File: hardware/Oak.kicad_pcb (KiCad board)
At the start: 2 copper layers, 100 x 40 mm, 69 parts, among them J1 18650 Battery holder, J2 USB_B_Micro, J4 Conn_ARM_JTAG_SWD_10, SW1 SW_SPDT, SW2 SW_Push, U1 AP2112, U2 ATSAMD21, U3 MCP7383, U4 PA1010D, U5 RFM95, U6 Waveshare_1in54_epaper

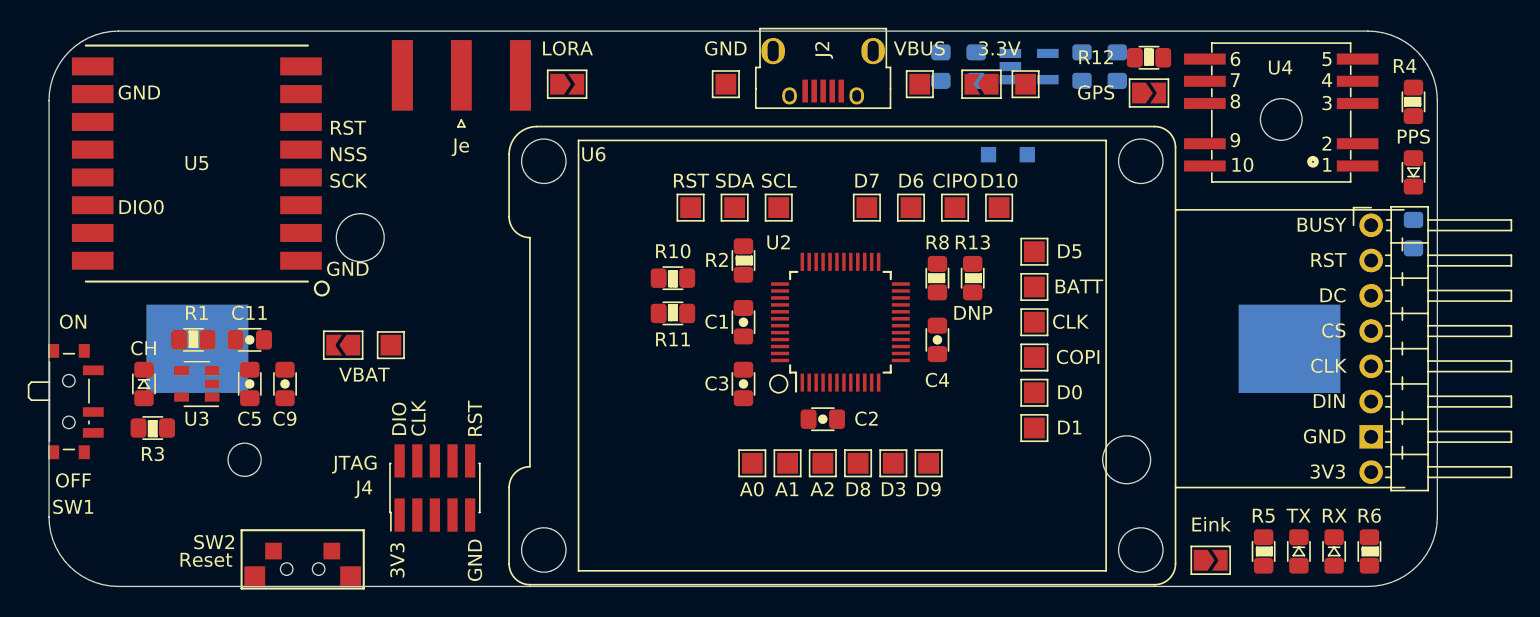
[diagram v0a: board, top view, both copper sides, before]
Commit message: feat: fix all clearance issues with local clearance settings
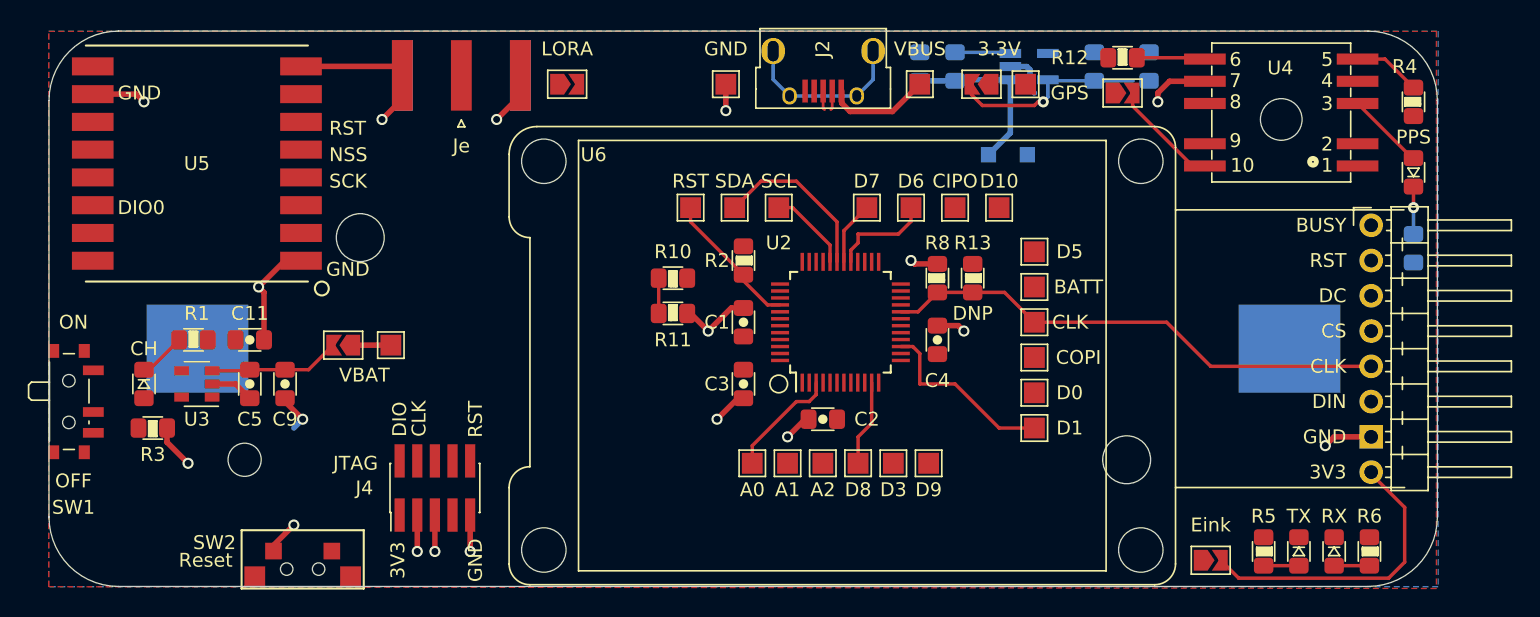
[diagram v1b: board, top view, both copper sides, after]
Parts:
- moved C7 2.29 mm to (172.7, 72.4)
- moved JP3 1.91 mm to (170.8, 74.3)
- moved R12 1.91 mm to (170.8, 71.8)
- moved C10 1.52 mm to (156.2, 72.4)
- moved R9 1.52 mm to (158.8, 72.4)
- moved R7 1.03 mm to (191.8, 85.5)
- moved C6 0.89 mm to (168.8, 72.4)
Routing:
- net GND: track 0.00 -> 73.1 mm, vias 0 -> 18
- net /CLK: track 0.00 -> 36.7 mm
- net Net-(JP5-Pad2): track 0.00 -> 21.7 mm
- net /VBUS: track 0.00 -> 20.2 mm
- net Net-(C6-Pad1): track 0.00 -> 14.3 mm, vias 0 -> 1
- net /D1: track 0.00 -> 13.3 mm
- net Net-(J2-Pad6): track 0.00 -> 12.3 mm
- net /SDA: track 0.00 -> 12.3 mm
- net /RST: track 0.00 -> 10.2 mm
- net Net-(C5-Pad2): track 0.00 -> 9.48 mm
- net /A0: track 0.00 -> 8.25 mm
- net Net-(JP3-Pad2): track 0.00 -> 7.93 mm
- net /D6: track 0.00 -> 7.40 mm
- net /D8: track 0.00 -> 6.22 mm
- net /SCL: track 0.00 -> 6.02 mm
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- added copper zone on F.Cu, net +3V3
- added copper zone on B.Cu, net GND

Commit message: feat: add inverted labels with more routes (33 unconnected). close #18
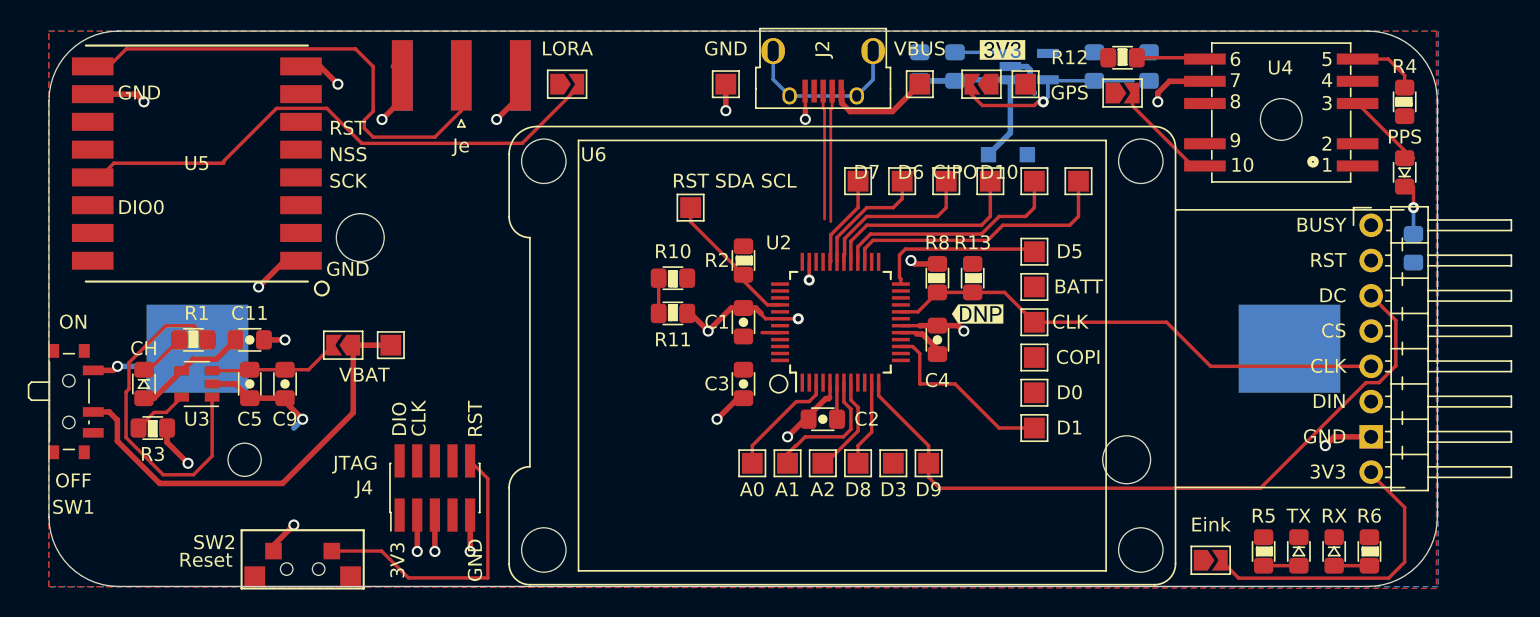
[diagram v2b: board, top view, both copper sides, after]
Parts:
- added svg2mod: G***, label, F.Cu at (160.4, 90.2)
- added svg2mod: G***, label, F.Cu at (162.2, 71.2)
- moved TP17 12.2 mm to (154.9, 80.6)
- moved TP19 6.02 mm to (158.1, 80.6)
- moved TP20 6.02 mm to (161.3, 80.6)
- moved TP21 6.02 mm to (164.5, 80.6)
- moved TP18 6.02 mm to (151.8, 80.6)
- moved TP22 6.02 mm to (167.6, 80.6)
- moved D3 0.64 mm to (191.1, 80.0)
- moved R4 0.64 mm to (191.1, 74.9)
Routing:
- net /D9: track 0.00 -> 51.7 mm
- net Net-(JP4-Pad2): track 0.00 -> 39.5 mm
- net Net-(J3-Pad1): track 0.00 -> 36.0 mm
- net /VBAT: track 2.70 -> 31.4 mm
- net Net-(R1-Pad2): track 0.00 -> 24.8 mm
- net /RST: track 10.2 -> 31.2 mm
- net /D10: track 0.00 -> 19.8 mm
- net /CIPO: track 0.00 -> 16.9 mm
- net /D5: track 0.00 -> 12.1 mm
- net /A1: track 0.00 -> 9.55 mm
- net GND: track 73.1 -> 82.4 mm, vias 18 -> 23
- net /VBUS: track 20.2 -> 28.5 mm
- net Net-(J1-Pad1): track 0.00 -> 8.15 mm, vias 0 -> 1
- net /USB_D-: track 1.38 -> 9.45 mm
- net /USB_D+: track 1.38 -> 9.26 mm
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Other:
- net class Power: clearance 0.3 -> 0.2
- board text removed: "3.3V"
- board text removed: "DNP"

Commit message: feat: add more routes (22 remaining unconnected)
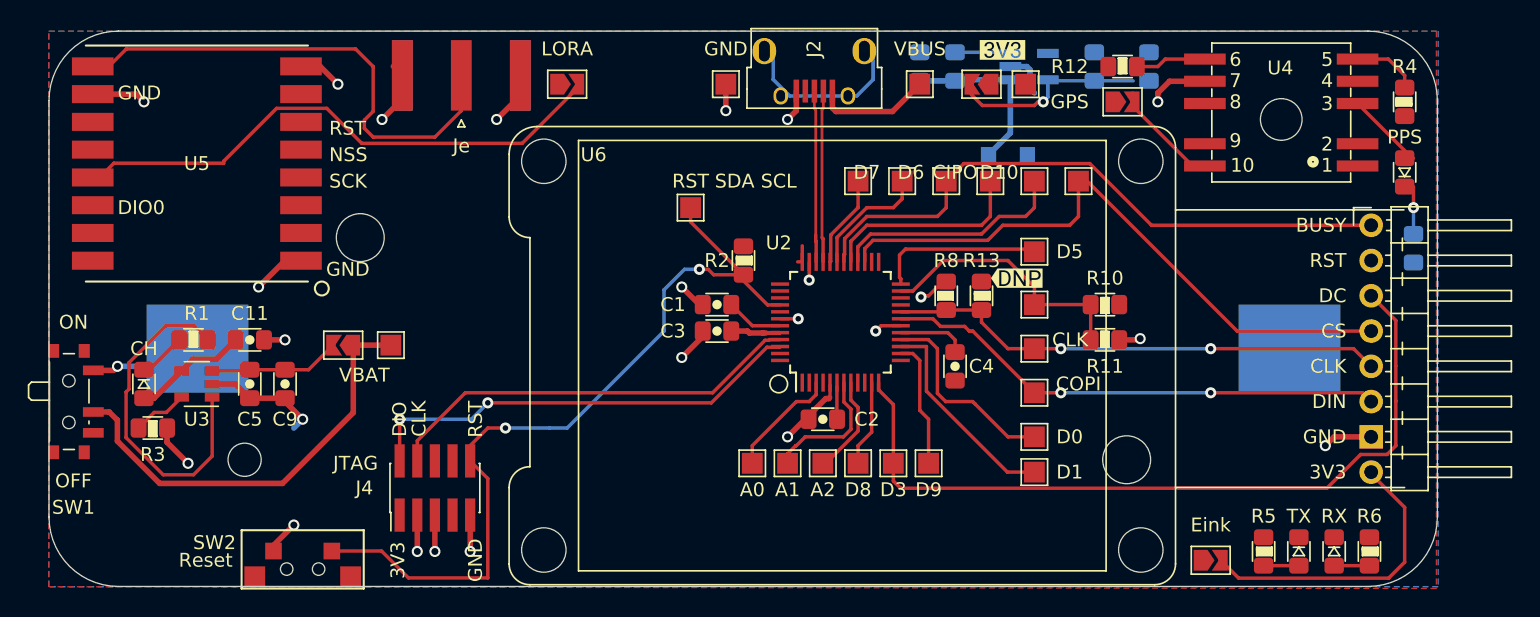
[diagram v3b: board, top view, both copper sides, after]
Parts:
- moved R10 31.2 mm to (169.5, 89.5)
- moved R11 31.2 mm to (169.5, 92.1)
- moved C3 4.26 mm to (141.6, 91.4), turned to 180 degrees
- moved svg2mod 3.82 mm to (163.2, 87.6)
- moved TP12 3.17 mm to (164.5, 101.6)
- moved TP13 3.17 mm to (164.5, 99.1)
- moved TP5 2.54 mm to (164.5, 95.9)
- moved TP10 2.54 mm to (154.3, 101.0)
- moved TP11 2.54 mm to (156.8, 101.0)
- moved C1 2.29 mm to (141.6, 89.5), turned to 0 degrees
- moved C4 2.29 mm to (158.8, 94.0), turned to 270 degrees
- moved TP16 1.90 mm to (164.5, 92.7)
- moved R8 1.42 mm to (158.1, 88.9)
- moved R13 1.42 mm to (160.7, 88.9)
- moved TP14 1.27 mm to (164.5, 89.5)
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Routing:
- net /COPI: track 0.00 -> 36.3 mm, vias 0 -> 2
- net /D7: track 11.8 -> 44.8 mm
- net /SWDIO: track 0.00 -> 32.6 mm, vias 0 -> 2
- net /SWCLK: track 0.00 -> 30.6 mm
- net /RST: track 31.2 -> 59.1 mm, vias 0 -> 2
- net /D10: track 19.8 -> 45.4 mm
- net /BATT: track 2.54 -> 19.2 mm
- net /D0: track 0.00 -> 14.4 mm
- net /D3: track 4.94 -> 14.5 mm
- net +3V3: track 6.76 -> 13.6 mm
- net GND: track 82.4 -> 76.7 mm, vias 23 -> 24
- net /D9: track 51.7 -> 56.7 mm
- net Net-(C1-Pad2): track 0.00 -> 4.14 mm
- net /USB_D+: track 9.26 -> 12.4 mm
- net /USB_D-: track 9.45 -> 12.4 mm
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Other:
- board text removed: "BATT"

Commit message: feat: add more routes (14 remaining unconnected)
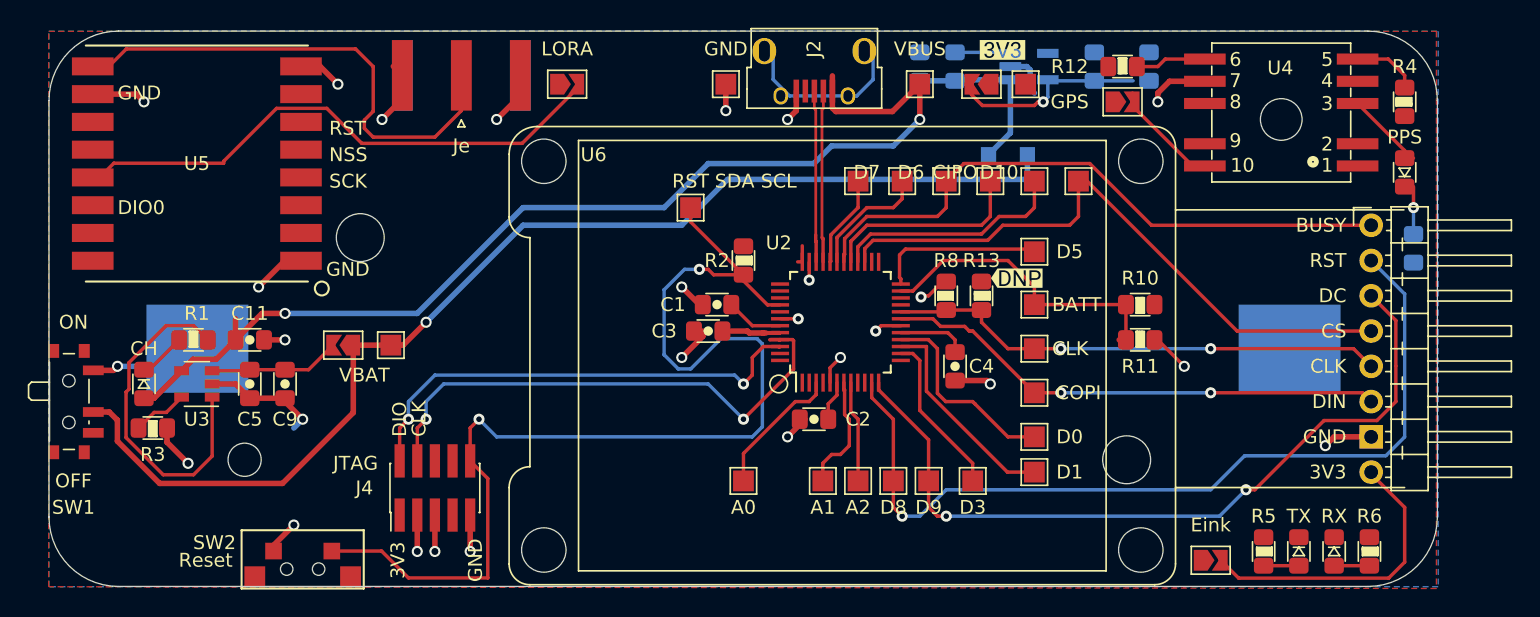
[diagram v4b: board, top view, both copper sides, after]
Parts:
- moved TP11 3.42 mm to (160.0, 102.2)
- moved TP9 2.84 mm to (154.3, 102.2)
- moved TP10 2.84 mm to (156.8, 102.2)
- moved TP6 2.84 mm to (151.8, 102.2)
- moved TP7 2.84 mm to (149.2, 102.2)
- moved R10 2.54 mm to (172.1, 89.5)
- moved R11 2.54 mm to (172.1, 92.1)
- moved TP8 1.42 mm to (143.5, 102.2)
- moved C2 0.63 mm to (148.6, 97.8)
- moved C3 0.63 mm to (141.0, 91.4)
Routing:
- net /VBUS: track 29.4 -> 90.4 mm, vias 0 -> 2
- net /D8: track 6.22 -> 62.8 mm, vias 0 -> 1
- net /VBAT: track 31.4 -> 84.0 mm, vias 0 -> 1
- net /RST: track 59.1 -> 82.5 mm
- net /SWCLK: track 30.6 -> 37.9 mm, vias 0 -> 2
- net /BATT: track 19.2 -> 22.0 mm
- net /D3: track 14.5 -> 17.1 mm
- net GND: track 76.7 -> 79.2 mm, vias 24 -> 26
- net /SWDIO: track 32.6 -> 34.3 mm
- net /A0: track 8.25 -> 9.83 mm
- net /A1: track 9.55 -> 8.40 mm
- net +3V3: track 13.6 -> 14.6 mm
- net /D9: track 56.7 -> 56.1 mm, vias 0 -> 2
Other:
- board text added: "BATT"

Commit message: feat: add more routes (11 remaining unconnected)
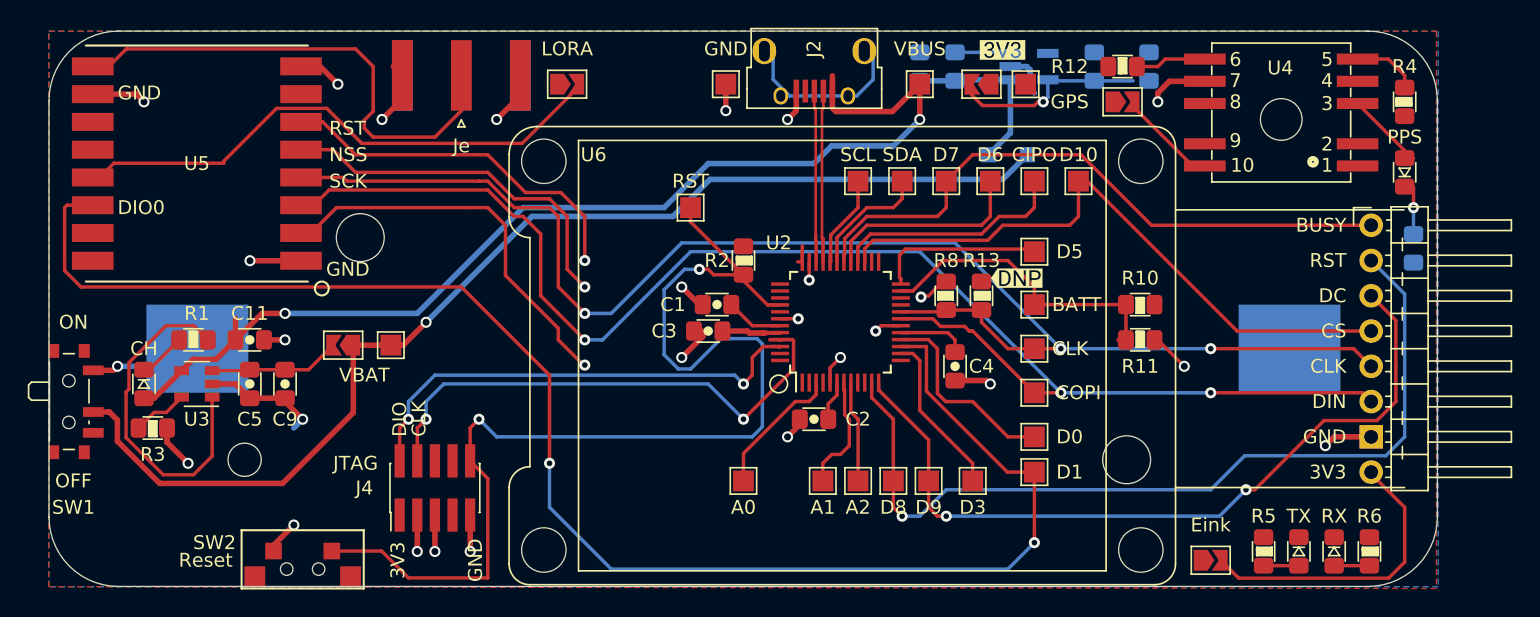
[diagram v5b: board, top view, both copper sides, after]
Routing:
- net /D1: track 15.2 -> 112.6 mm, vias 0 -> 2
- net /COPI: track 36.3 -> 105.9 mm, vias 2 -> 3
- net /CLK: track 36.1 -> 103.6 mm, vias 2 -> 3
- net /CIPO: track 16.9 -> 45.9 mm, vias 0 -> 1
- net /D5: track 12.1 -> 39.4 mm, vias 0 -> 1
- net /D6: track 14.8 -> 41.7 mm, vias 0 -> 1
- net /VBAT: track 84.0 -> 83.0 mm
- net /D7: track 44.8 -> 45.3 mm
- net GND: track 79.2 -> 79.7 mm

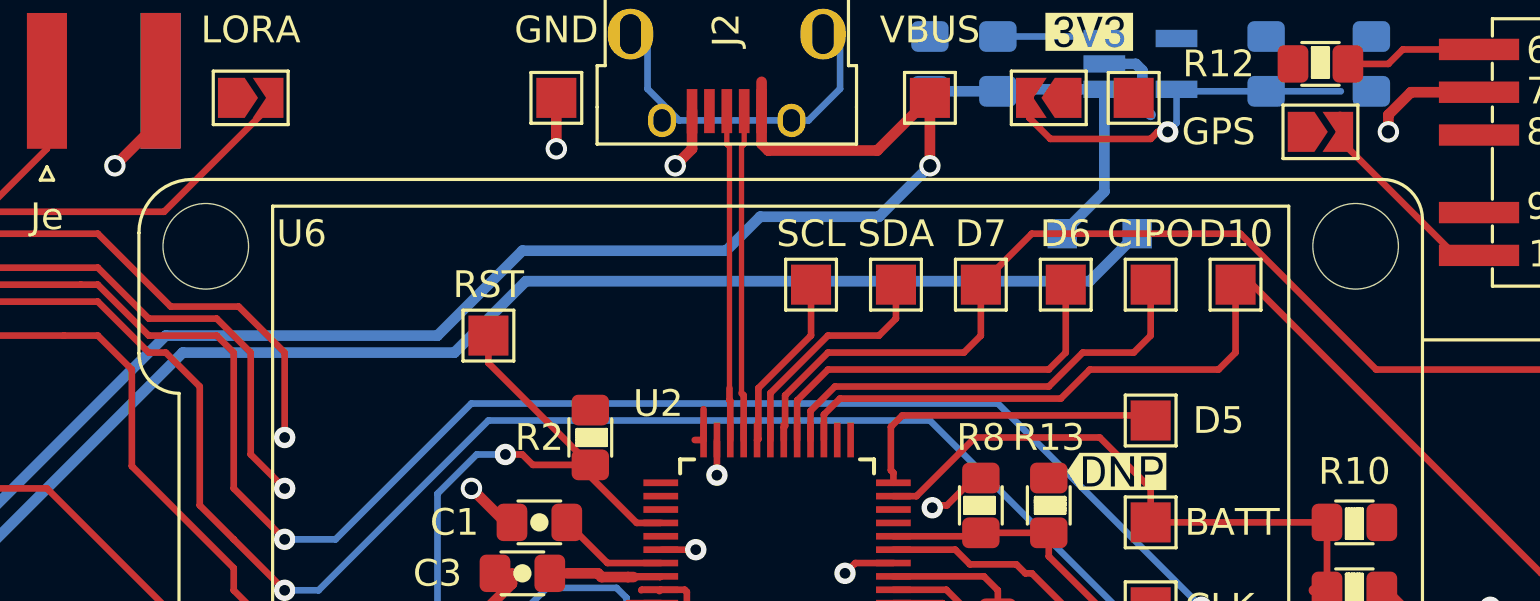
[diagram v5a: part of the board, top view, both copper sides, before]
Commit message: feat: add more routes (10 remaining unconnected)
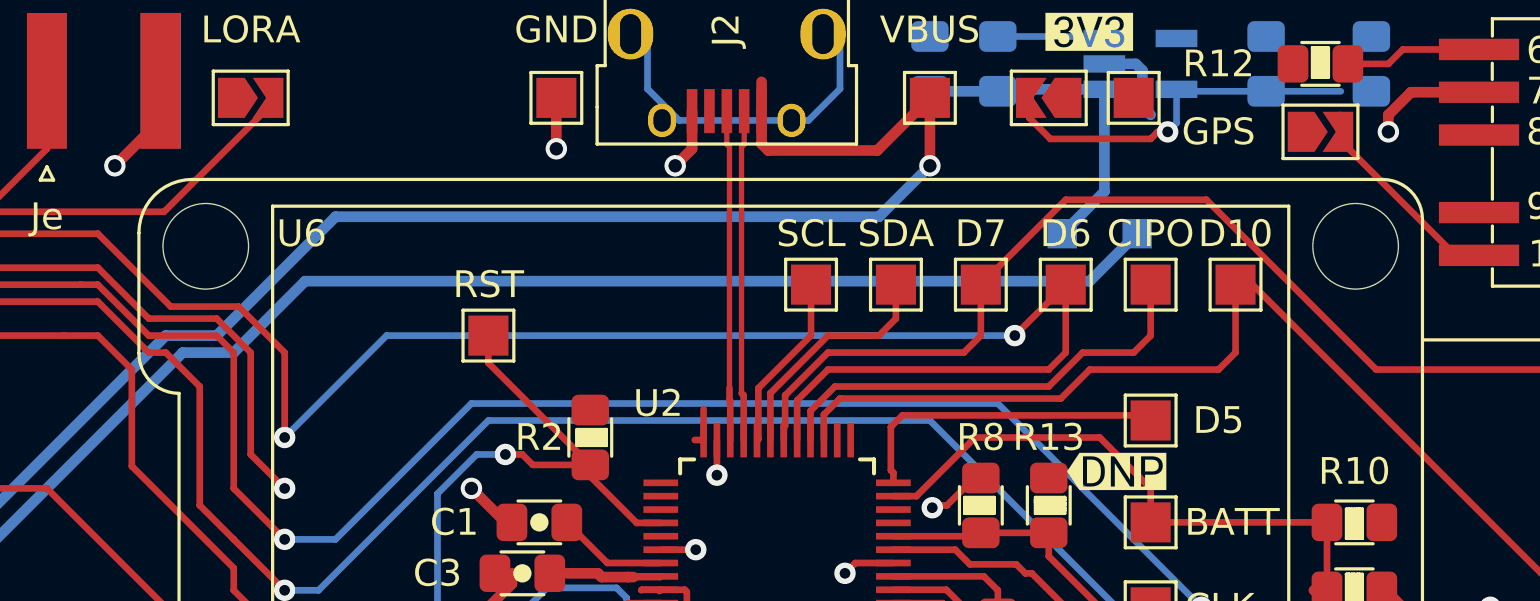
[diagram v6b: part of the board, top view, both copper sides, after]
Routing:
- net /D6: track 41.7 -> 73.3 mm, vias 1 -> 2
- net /D7: track 45.3 -> 46.4 mm
